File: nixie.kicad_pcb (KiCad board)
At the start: 2 copper layers, 200 x 60 mm, 65 parts, among them J1 Barrel_Jack, Q1 2N3906, Q2 IRF644, SW1 RotaryEncoder_Switch, U1 4504, U2 MC34063AP, U3 HV5222PG-G, U4 LM7805_TO220, U5 HV5222PG-G, U6 ATmega328P-P, U7 DS3231MZ

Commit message: pcb layout updated
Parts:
- added H1: MountingHole_Pad, MountingHole:MountingHole_3.2mm_M3_Pad_Via, F.Cu at (76.0, 65.0)
- added H2: MountingHole_Pad, MountingHole:MountingHole_3.2mm_M3_Pad_Via, F.Cu at (258.0, 65.0)
- added H3: MountingHole_Pad, MountingHole:MountingHole_3.2mm_M3_Pad_Via, F.Cu at (237.0, 111.0)
- added H4: MountingHole_Pad, MountingHole:MountingHole_3.2mm_M3_Pad_Via, F.Cu at (97.0, 111.0)
- U4: footprint Package_TO_SOT_THT:TO-220-3_Vertical -> Package_TO_SOT_THT:TO-220-3_Horizontal_TabDown
- moved C15 182.9 mm to (255.5, 80.5), turned to 90 degrees
- moved R23 180.4 mm to (248.4, 83.5)
- moved R21 167.0 mm to (237.5, 83.5)
- moved R19 162.0 mm to (226.4, 66.0)
- moved C13 158.6 mm to (229.0, 76.5)
- moved C12 158.3 mm to (229.0, 73.0)
- moved R20 155.4 mm to (226.5, 83.5)
- moved C7 154.9 mm to (145.0, 68.0)
- moved R16 154.2 mm to (226.4, 69.5)
- moved R18 153.2 mm to (226.5, 80.0)
- moved C4 147.7 mm to (145.0, 73.0)
- moved D2 125.6 mm to (106.7, 66.5), turned to 180 degrees
- moved C2 99.3 mm to (77.6, 82.5), turned to 180 degrees
- moved J1 93.3 mm to (74.5, 71.0), turned to 90 degrees
- moved C1 88.9 mm to (77.1, 74.5), turned to -90 degrees
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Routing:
- net Net-(R18-Pad2): track 0.00 -> 2.47 mm
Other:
- board size 200 x 60 mm -> 190 x 55 mm
- copper layers 2 -> 4

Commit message: pcb layout update
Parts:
- moved J1 53.7 mm to (127.6, 63.6)
- moved U6 34.3 mm to (224.6, 70.6)
- moved C11 33.6 mm to (228.8, 76.6)
- moved C6 16.6 mm to (164.7, 83.6), turned to 180 degrees
- moved U1 13.5 mm to (168.2, 87.0), turned to -90 degrees
- moved C15 12.8 mm to (258.4, 93.0), turned to -90 degrees
- moved R16 8.70 mm to (232.6, 75.6)
- moved R19 8.70 mm to (232.6, 72.1)
- moved C12 8.70 mm to (235.2, 79.1)
- moved C13 8.70 mm to (235.2, 82.6)
- moved R18 8.70 mm to (232.7, 86.1)
- moved SW1 8.70 mm to (243.7, 79.3)
- moved C8 8.41 mm to (168.1, 97.5), turned to 180 degrees
- moved R20 7.62 mm to (230.9, 89.7)
- moved BT1 7.58 mm to (176.9, 91.3)
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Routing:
- net Net-(U3-DATA_OUT): track 0.00 -> 90.3 mm, vias 0 -> 2
- net Net-(U1-Aout): track 0.00 -> 86.5 mm, vias 0 -> 3
- net Net-(U1-Bout): track 0.00 -> 85.5 mm, vias 0 -> 3
- net /D16: track 0.00 -> 80.4 mm
- net /D15: track 0.00 -> 74.1 mm
- net ROT_PSH: track 0.00 -> 73.9 mm
- net SQW: track 0.00 -> 73.8 mm, vias 0 -> 2
- net /D229: track 0.00 -> 71.5 mm, vias 0 -> 2
- net /D14: track 0.00 -> 68.8 mm
- net /D230: track 0.00 -> 66.5 mm, vias 0 -> 2
- net /D13: track 0.00 -> 63.3 mm
- net /D231: track 0.00 -> 62.9 mm, vias 0 -> 2
- net /D17: track 0.00 -> 61.5 mm, vias 0 -> 1
- net /D18: track 0.00 -> 59.2 mm, vias 0 -> 1
- net /D232: track 0.00 -> 59.1 mm, vias 0 -> 2
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- added copper zone on B.Cu, net 5V
- added copper zone on F.Cu, net 5V
- added copper zone on In1.Cu, net GND
- added copper zone on In2.Cu, net GND
- added copper zone on B.Cu, net HV
- added copper zone on F.Cu, net HV
- added copper zone on B.Cu, net Vin
- added copper zone on F.Cu, net Vin
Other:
- board size 190 x 55 mm -> 189.5 x 55 mm

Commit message: pcb layout update
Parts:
- added J2: Conn_01x02_Pin, Connector_PinHeader_2.54mm:PinHeader_1x02_P2.54mm_Vertical, F.Cu at (77.5, 71.2)
- J1: footprint Connector_PinHeader_2.54mm:PinHeader_1x02_P2.54mm_Vertical -> TerminalBlock_Phoenix:TerminalBlock_Phoenix_MKDS-1,5-2-5.08_1x02_P5.08mm_Horizontal; moved to B.Cu
- moved J1 4.88 mm to (131.0, 67.1), turned to 180 degrees
- moved C4 3.60 mm to (141.6, 77.0)
- moved C7 3.60 mm to (141.6, 72.0)
- moved U4 3.60 mm to (138.6, 76.9)
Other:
- board text added: "Nixie Clock | Pim Borman version 1.0 https://github.com/pimborman"
- board text added: "PIM BORMAN FECIT"
- board text added: "TEMPUS FUGIT"

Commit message: pcb layout update
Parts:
- moved J2 0.20 mm to (77.5, 71.4)
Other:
- board text added: "Nixie Clock | Pim Borman version 1.0 https://github.com/pimborman/nixie-clock"
- board text removed: "Nixie Clock | Pim Borman version 1.0 https://github.com/pimborman"
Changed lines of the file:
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@@
 		(tags "CP Radial series Radial pin pitch 2.50mm  diameter 6.3mm Electrolytic Capacitor")
 		(property "Reference" "C5"
-			(at -3.1 -0.08 180)
+			(at -2.9 1.12 180)
 			(layer "F.SilkS")
 			(effects
@@
 		)
 		(property "Value" "100u"
-			(at 3.9 4.12 180)
+			(at -2.9 -2.08 180)
 			(layer "F.SilkS")
 			(effects
@@
 		(tags "mounting hole 3.2mm m3")
 		(property "Reference" "H1"
-			(at -1.2 4.4 0)
+			(at 4 -2.6 0)
 			(layer "F.SilkS")
 			(effects
@@
 	(footprint "Connector_PinHeader_2.54mm:PinHeader_1x02_P2.54mm_Vertical"
 		(layer "F.Cu")
-		(at 77.475 71.2 -90)
+		(at 77.475 71.4 -90)
 		(descr "Through hole straight pin header, 1x02, 2.54mm pitch, single row")
 		(tags "Through hole pin header THT 1x02 2.54mm single row")
 		(property "Reference" "J2"
-			(at 0 -2.33 90)
+			(at 2.4 3.475 0)
 			(layer "F.SilkS")
 			(effects
@@
 		)
 		(property "Value" "Conn_01x02_Pin"
-			(at 0 4.87 90)
+			(at 0 8.875 90)
 			(layer "F.Fab")
 			(effects
@@
 		)
 		(fp_text user "${REFERENCE}"
-			(at 0 1.270001 360)
+			(at 0 1.270001 0)
 			(layer "F.Fab")
 			(effects
@@
 		(tags "C Disc series Radial pin pitch 5.00mm  diameter 4.7mm width 2.5mm Capacitor")
 		(property "Reference" "C1"
-			(at -1.9 -0.08 180)
+			(at 2.5 2.32 -90)
 			(layer "F.SilkS")
 			(effects
@@
 		(tags "THT Terminal Block Phoenix MKDS-1,5-2-5.08 pitch 5.08mm size 10.2x9.8mm^2 drill 1.3mm pad 2.6mm")
 		(property "Reference" "J1"
-			(at 2.54 6.26 0)
+			(at 3 -5.695 0)
 			(layer "B.SilkS")
 			(effects
@@
 		(layer "Edge.Cuts")
 	)
-	(gr_text "Nixie Clock | Pim Borman\nversion 1.0\nhttps://github.com/pimborman\n\n"
+	(gr_text "Nixie Clock | Pim Borman\nversion 1.0\nhttps://github.com/pimborman/nixie-clock\n\n"
 		(at 252 69.2 0)
 		(layer "B.SilkS")

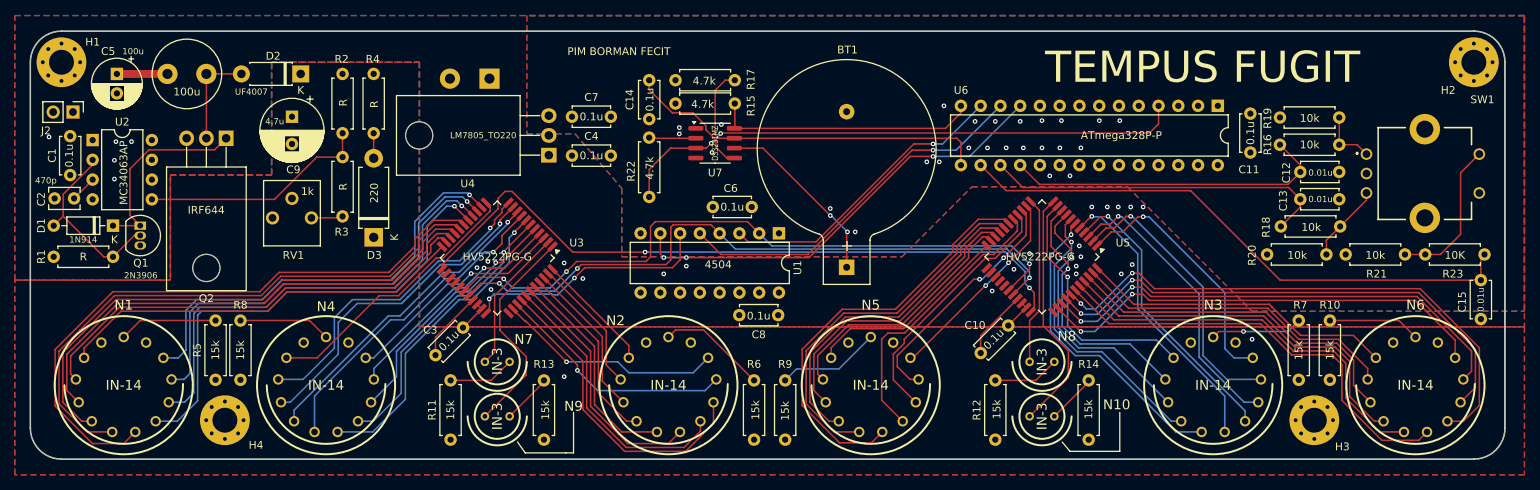
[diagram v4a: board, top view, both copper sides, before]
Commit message: thicker smps traces
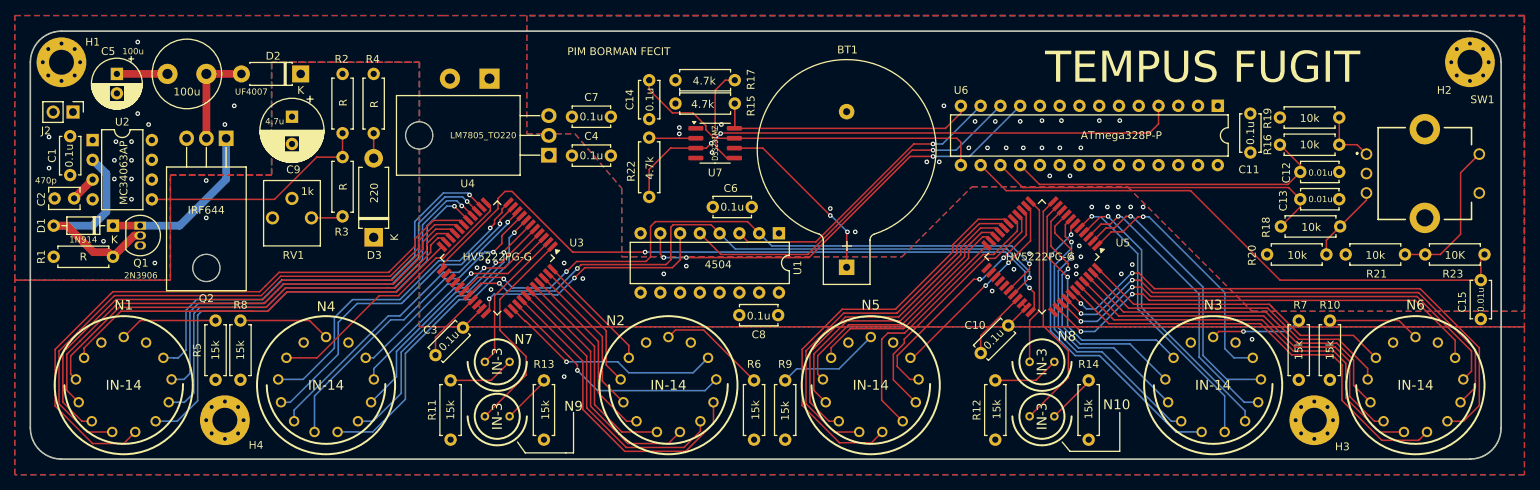
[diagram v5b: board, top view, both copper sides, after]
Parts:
- moved H2 0.50 mm to (257.0, 65.0)
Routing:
- net Net-(D1-A): track 23.7 -> 28.8 mm
- net Net-(D1-K): track 25.3 -> 22.4 mm
- net GND: vias 42 -> 55
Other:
- board size 189.5 x 55 mm -> 189 x 55 mm
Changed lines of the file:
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@@
 	(title_block
 		(title "Nixie Clock Project")
-		(date "2024-09-24")
-		(rev "0.1")
+		(date "2024-10-03")
+		(rev "1.0")
 		(company "Pim Borman")
 	)
@@
 			(outputformat 1)
 			(mirror no)
-			(drillshape 1)
+			(drillshape 0)
 			(scaleselection 1)
 			(outputdirectory "")
@@
 	(footprint "MountingHole:MountingHole_3.2mm_M3_Pad_Via"
 		(layer "F.Cu")
-		(at 257.5 65)
+		(at 257 65)
 		(descr "Mounting Hole 3.2mm, M3")
 		(tags "mounting hole 3.2mm m3")
@@
 	(gr_line
 		(start 76 116)
-		(end 257.5 116)
+		(end 257 116)
 		(locked yes)
 		(stroke
@@
 	)
 	(gr_arc
-		(start 261.5 112)
-		(mid 260.328427 114.828427)
-		(end 257.5 116)
+		(start 261 112)
+		(mid 259.828427 114.828427)
+		(end 257 116)
 		(locked yes)
 		(stroke
@@
 	)
 	(gr_line
-		(start 257.5 61)
+		(start 257 61)
 		(end 76 61)
 		(locked yes)
@@
 	)
 	(gr_line
-		(start 261.5 112)
-		(end 261.5 65)
+		(start 261 112)
+		(end 261 65)
 		(locked yes)
 		(stroke
@@
 	)
 	(gr_arc
-		(start 257.5 61)
-		(mid 260.328427 62.171573)
-		(end 261.5 65)
+		(start 257 61)
+		(mid 259.828427 62.171573)
+		(end 261 65)
 		(locked yes)
 		(stroke
@@
 	)
 	(via
+		(at 85.8 71.6)
+		(size 0.6)
+		(drill 0.3)
+		(layers "F.Cu" "B.Cu")
+		(free yes)
+		(net 1)
+	)
+	(via
 		(at 159.6 76.6)
 		(size 0.6)
@@
 	)
 	(via
+		(at 85 77.6)
+		(size 0.6)
+		(drill 0.3)
+		(layers "F.Cu" "B.Cu")
+		(free yes)
+		(net 1)
+	)
+	(via
 		(at 211.8 83.6)
 		(size 0.6)
@@
 	)
 	(via
+		(at 85.8 62.4)
+		(size 0.6)
+		(drill 0.3)
+		(layers "F.Cu" "B.Cu")
+		(free yes)
+		(net 1)
+	)
+	(via
+		(at 87.2 73)
+		(size 0.6)
+		(drill 0.3)
+		(layers "F.Cu" "B.Cu")
+		(free yes)
+		(net 1)
+	)
+	(via
 		(at 83 75.2)
 		(size 0.6)
@@
 	)
 	(via
+		(at 94.6 85)
+		(size 0.6)
+		(drill 0.3)
+		(layers "F.Cu" "B.Cu")
+		(free yes)
+		(net 1)
+	)
+	(via
 		(at 200.4 89.6)
 		(size 0.6)
@@
 	)
 	(via
+		(at 81.4 88)
+		(size 0.6)
+		(drill 0.3)
+		(layers "F.Cu" "B.Cu")
+		(free yes)
+		(net 1)
+	)
+	(via
 		(at 213.6 91)
 		(size 0.6)
@@
 	)
 	(via
+		(at 98.2 70.6)
+		(size 0.6)
+		(drill 0.3)
+		(layers "F.Cu" "B.Cu")
+		(free yes)
+		(net 1)
+	)
+	(via
 		(at 178 86.8)
 		(size 0.6)
@@
 	)
 	(via
+		(at 74.4 78.6)
+		(size 0.6)
+		(drill 0.3)
+		(layers "F.Cu" "B.Cu")
+		(free yes)
+		(net 1)
+	)
+	(via
 		(at 206.8 88.6)
 		(size 0.6)
@@
 	)
 	(via
+		(at 85 80)
+		(size 0.6)
+		(drill 0.3)
+		(layers "F.Cu" "B.Cu")
+		(free yes)
+		(net 1)
+	)
+	(via
 		(at 192.6 76)
 		(size 0.6)
@@
 	)
 	(via
+		(at 85 82.6)
+		(size 0.6)
+		(drill 0.3)
+		(layers "F.Cu" "B.Cu")
+		(free yes)
+		(net 1)
+	)
+	(via
 		(at 187.2 77.8)
 		(size 0.6)
@@
 	)
 	(via
+		(at 97 73)
+		(size 0.6)
+		(drill 0.3)
+		(layers "F.Cu" "B.Cu")
+		(free yes)
+		(net 1)
+	)
+	(via
+		(at 88 90.8)
+		(size 0.6)
+		(drill 0.3)
+		(layers "F.Cu" "B.Cu")
+		(free yes)
+		(net 1)
+	)
+	(via
+		(at 94.6 80.2)
+		(size 0.6)
+		(drill 0.3)
+		(layers "F.Cu" "B.Cu")
+		(free yes)
+		(net 1)
+	)
+	(via
 		(at 193.4 72.6)
 		(size 0.6)
@@
 	)
 	(segment
+		(start 77.62 82.46)
+		(end 80 80.08)
+		(width 1)
+		(layer "F.Cu")
+		(net 4)
+	)
+	(segment
 		(start 80 80.12)
 		(end 80 80.08)
@@
 	(segment
 		(start 77.62 82.5)
-		(end 80 80.12)
-		(width 0.2)
+		(end 77.62 82.46)
+		(width 1)
 		(layer "F.Cu")
 		(net 4)
@@
 	)
 	(segment
-		(start 80 78.175635)
-		(end 80 77.54)
-		(width 0.2)
+		(start 85.35 87.27)
+		(end 86.12 87.27)
+		(width 1)
 		(layer "F.Cu")
 		(net 10)
 	)
 	(segment
-		(start 85.35 87.27)
-		(end 86.12 87.27)
-		(width 0.2)
+		(start 76.7 86)
+		(end 78.735 88.035)
+		(width 1)
 		(layer "F.Cu")
 		(net 10)
 	)
 	(segment
-		(start 76.22 84.78)
-		(end 81.44 90)
-		(width 0.2)
+		(start 82.025 89.405)
+		(end 82.62 90)
+		(width 1)
 		(layer "F.Cu")
 		(net 10)
 	)
 	(segment
-		(start 82.62 90)
-		(end 85.35 87.27)
-		(width 0.2)
+		(start 75 86)
+		(end 76.7 86)
+		(width 1)
 		(layer "F.Cu")
 		(net 10)
 	)
 	(segment
-		(start 76.22 84.78)
-		(end 76.22 81.955635)
-		(width 0.2)
+		(start 78.735 88.035)
+		(end 80.105 89.405)
+		(width 1)
 		(layer "F.Cu")
 		(net 10)
 	)
 	(segment
-		(start 81.44 90)
-		(end 82.62 90)
-		(width 0.2)
+		(start 82.62 90)
+		(end 85.35 87.27)
+		(width 1)
 		(layer "F.Cu")
 		(net 10)
 	)
 	(segment
-		(start 76.22 81.955635)
-		(end 80 78.175635)
-		(width 0.2)
+		(start 80.105 89.405)
+		(end 82.025 89.405)
+		(width 1)
 		(layer "F.Cu")
 		(net 10)
 	)
 	(segment
-		(start 75 86)
-		(end 76.22 84.78)
-		(width 0.2)
-		(layer "F.Cu")
+		(start 81.77 79.31)
+		(end 81.77 84.23)
+		(width 1)
+		(layer "B.Cu")
 		(net 10)
 	)
 	(segment
-		(start 95.68 76.25)
-		(end 87.25 76.25)
-		(width 0.2)
-		(layer "F.Cu")
-		(net 11)
+		(start 80 77.54)
+		(end 81.77 79.31)
+		(width 1)
+		(layer "B.Cu")
+		(net 10)
 	)
 	(segment
-		(start 87.25 76.25)
-		(end 84.8 78.7)
-		(width 0.2)
-		(layer "F.Cu")
-		(net 11)
+		(start 81.77 84.23)
+		(end 80 86)
+		(width 1)
+		(layer "B.Cu")
+		(net 10)
 	)
 	(segment
-		(start 84.8 84.68)
+		(start 80 86)
+		(end 75 86)
+		(width 1)
+		(layer "B.Cu")
+		(net 10)
+	)
+	(segment
+		(start 82.62 86)
 		(end 86.12 86)
-		(width 0.2)
+		(width 1)
 		(layer "F.Cu")
 		(net 11)
 	)
 	(segment
-		(start 84.8 78.7)
-		(end 84.8 84.68)
-		(width 0.2)
+		(start 82.58 85.96)
+		(end 82.58 85.87)
+		(width 1)
 		(layer "F.Cu")
 		(net 11)
@@
 	(segment
 		(start 82.62 86)
-		(end 86.12 86)
-		(width 0.2)
+		(end 82.58 85.96)
+		(width 1)
 		(layer "F.Cu")
 		(net 11)
 	)
 	(segment
+		(start 97.16 80.03)
+		(end 91.19 86)
+		(width 1)
+		(layer "B.Cu")
+		(net 11)
+	)
+	(segment
 		(start 97.16 74.77)
-		(end 95.68 76.25)
-		(width 0.2)
-		(layer "F.Cu")
+		(end 97.16 80.03)
+		(width 1)
+		(layer "B.Cu")
+		(net 11)
+	)
+	(segment
+		(start 91.19 86)
+		(end 86.12 86)
+		(width 1)
+		(layer "B.Cu")
 		(net 11)
 	)
@@
 		(start 94.62 66.5)
 		(end 94.62 74.77)
-		(width 0.2)
+		(width 1)
 		(layer "F.Cu")
 		(net 12)
@@
 		(start 94.62 66.5)
 		(end 99.12 66.5)
-		(width 0.2)
+		(width 1)
 		(layer "F.Cu")
 		(net 12)

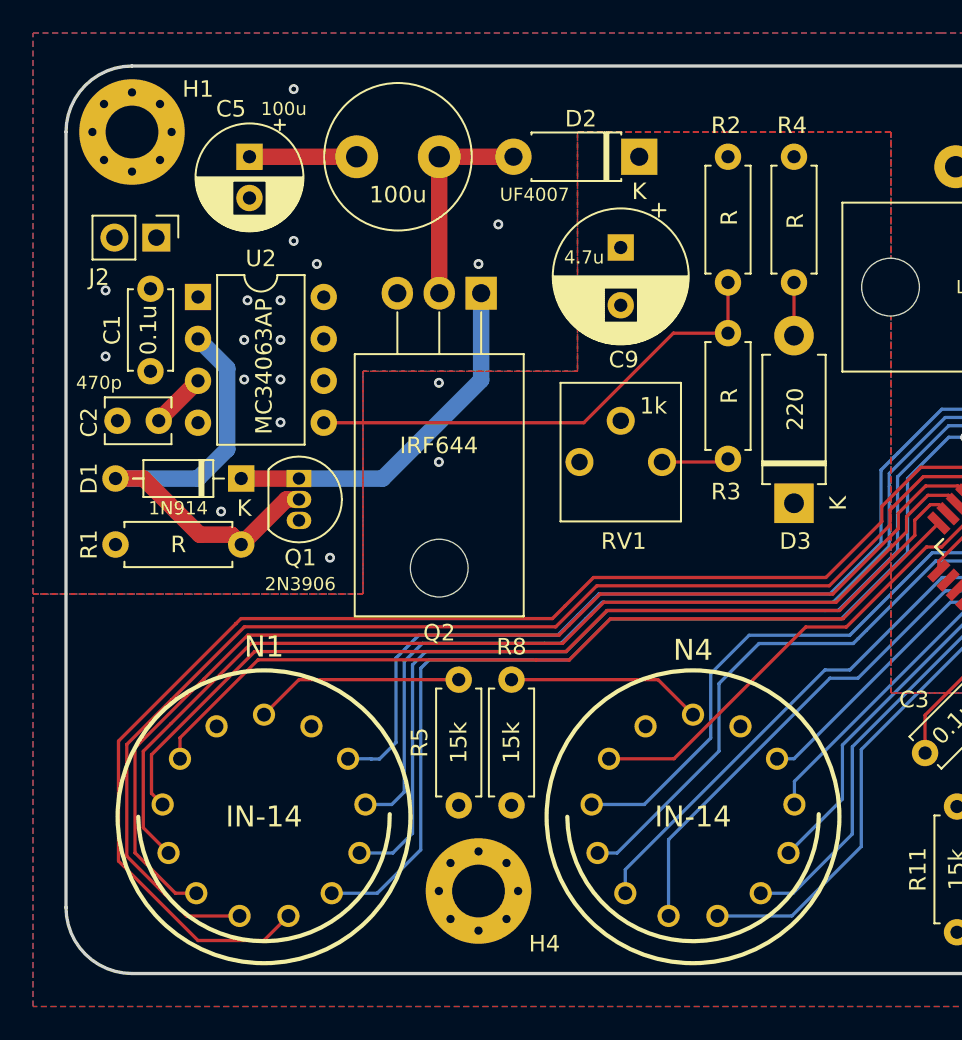
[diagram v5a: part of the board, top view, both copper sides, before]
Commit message: added a few stitching HV vias
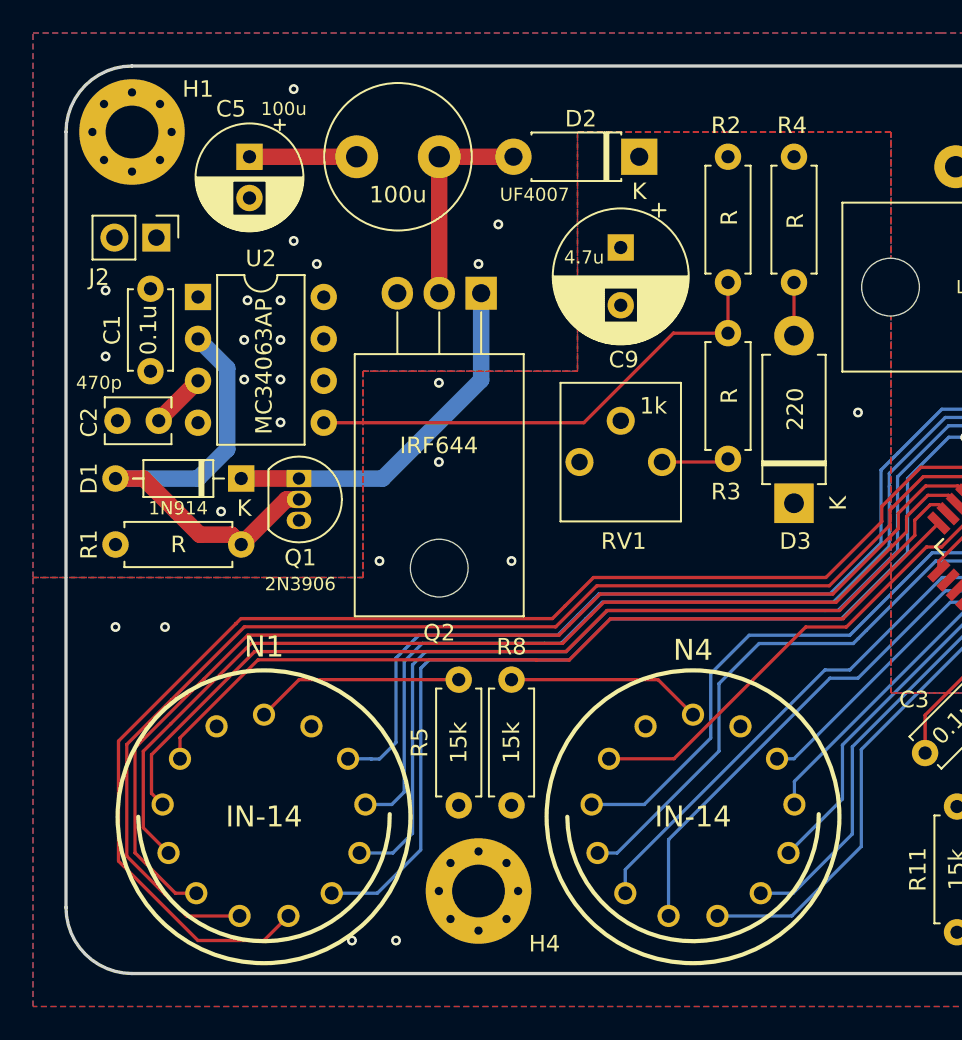
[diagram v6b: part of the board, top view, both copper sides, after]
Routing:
- net HV: vias 0 -> 7
- net GND: vias 55 -> 54
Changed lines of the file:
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@@
 	)
 	(via
-		(at 88 90.8)
-		(size 0.6)
-		(drill 0.3)
-		(layers "F.Cu" "B.Cu")
-		(free yes)
-		(net 1)
-	)
-	(via
 		(at 94.6 80.2)
 		(size 0.6)
@@
 		(net 5)
 	)
+	(via
+		(at 78 95)
+		(size 0.6)
+		(drill 0.3)
+		(layers "F.Cu" "B.Cu")
+		(free yes)
+		(net 6)
+	)
+	(via
+		(at 89.33 114)
+		(size 0.6)
+		(drill 0.3)
+		(layers "F.Cu" "B.Cu")
+		(free yes)
+		(net 6)
+	)
+	(via
+		(at 91 91)
+		(size 0.6)
+		(drill 0.3)
+		(layers "F.Cu" "B.Cu")
+		(free yes)
+		(net 6)
+	)
+	(via
+		(at 120 82)
+		(size 0.6)
+		(drill 0.3)
+		(layers "F.Cu" "B.Cu")
+		(free yes)
+		(net 6)
+	)
+	(via
+		(at 99 91)
+		(size 0.6)
+		(drill 0.3)
+		(layers "F.Cu" "B.Cu")
+		(free yes)
+		(net 6)
+	)
+	(via
+		(at 75 95)
+		(size 0.6)
+		(drill 0.3)
+		(layers "F.Cu" "B.Cu")
+		(free yes)
+		(net 6)
+	)
+	(via
+		(at 92 114)
+		(size 0.6)
+		(drill 0.3)
+		(layers "F.Cu" "B.Cu")
+		(free yes)
+		(net 6)
+	)
 	(segment
 		(start 233.6 80.7)
@@
 		(polygon
 			(pts
-				(xy 122 99) (xy 264 99) (xy 264 118) (xy 70 118) (xy 70 93) (xy 90 93) (xy 90 79.5) (xy 103 79.5)
+				(xy 122 99) (xy 264 99) (xy 264 118) (xy 70 118) (xy 70 92) (xy 90 92) (xy 90 79.5) (xy 103 79.5)
 				(xy 103 65) (xy 122 65)
 			)
@@
 		(polygon
 			(pts
-				(xy 264 99) (xy 122 99) (xy 122 65) (xy 103 65) (xy 103 79.5) (xy 90 79.5) (xy 90 93) (xy 70 93)
+				(xy 264 99) (xy 122 99) (xy 122 65) (xy 103 65) (xy 103 79.5) (xy 90 79.5) (xy 90 92) (xy 70 92)
 				(xy 70 59) (xy 125 59) (xy 264 59)
 			)
